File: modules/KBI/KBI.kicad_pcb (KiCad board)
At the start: 2 copper layers, 100 x 130 mm, 45 parts, among them IC3 µA741C, IC4 µA741C, J1 +15V, J2 -15V, J3 GND, J4 KOV, J5 GATE, J6 FM, P1 1M, P2 100k, P3 100k, P4 100k, P5 100k, T1 N-FET, T2 N-FET, T3 N-FET, T4 N-FET

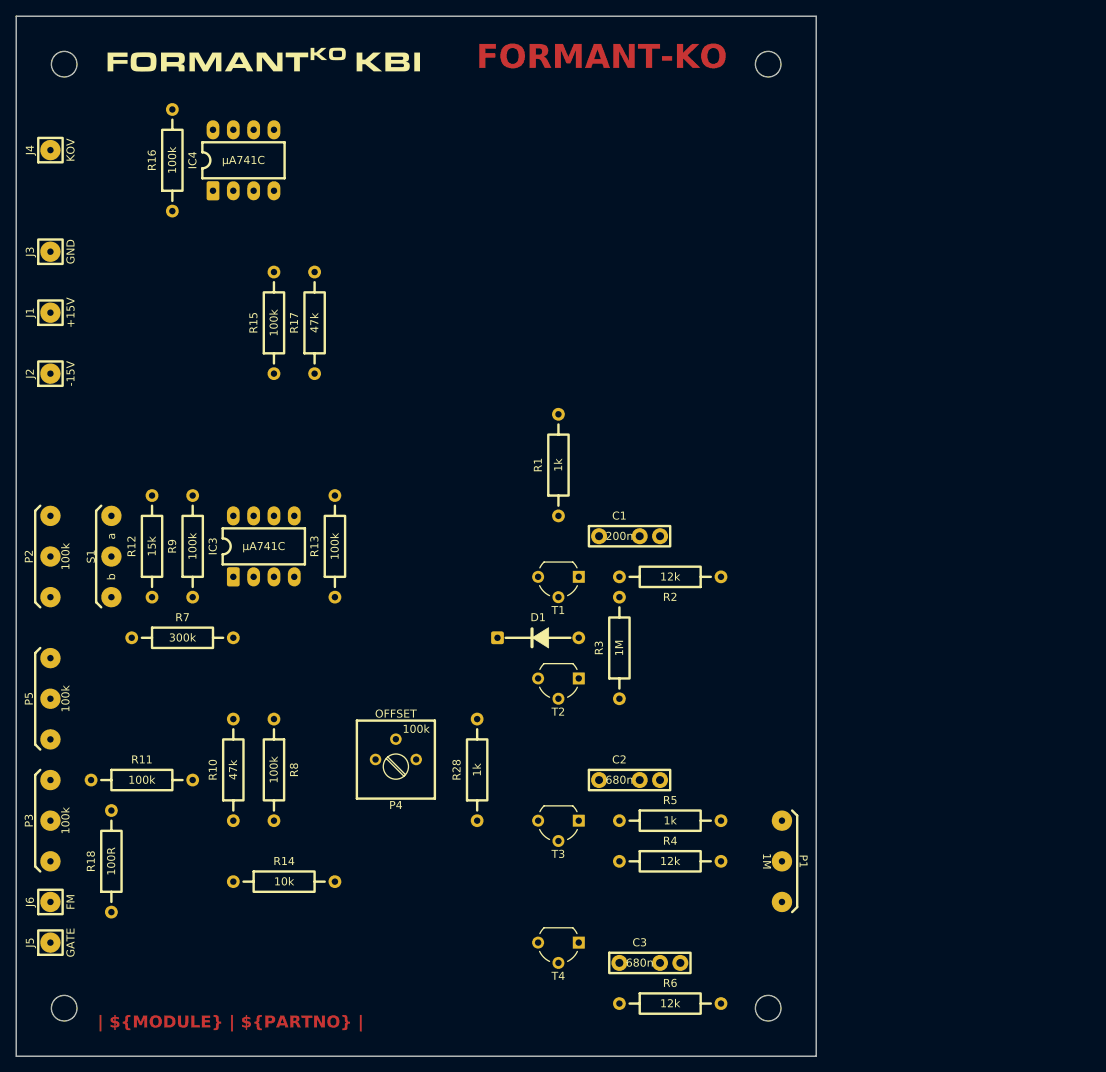
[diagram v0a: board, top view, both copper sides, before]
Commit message: initialized 6U modules
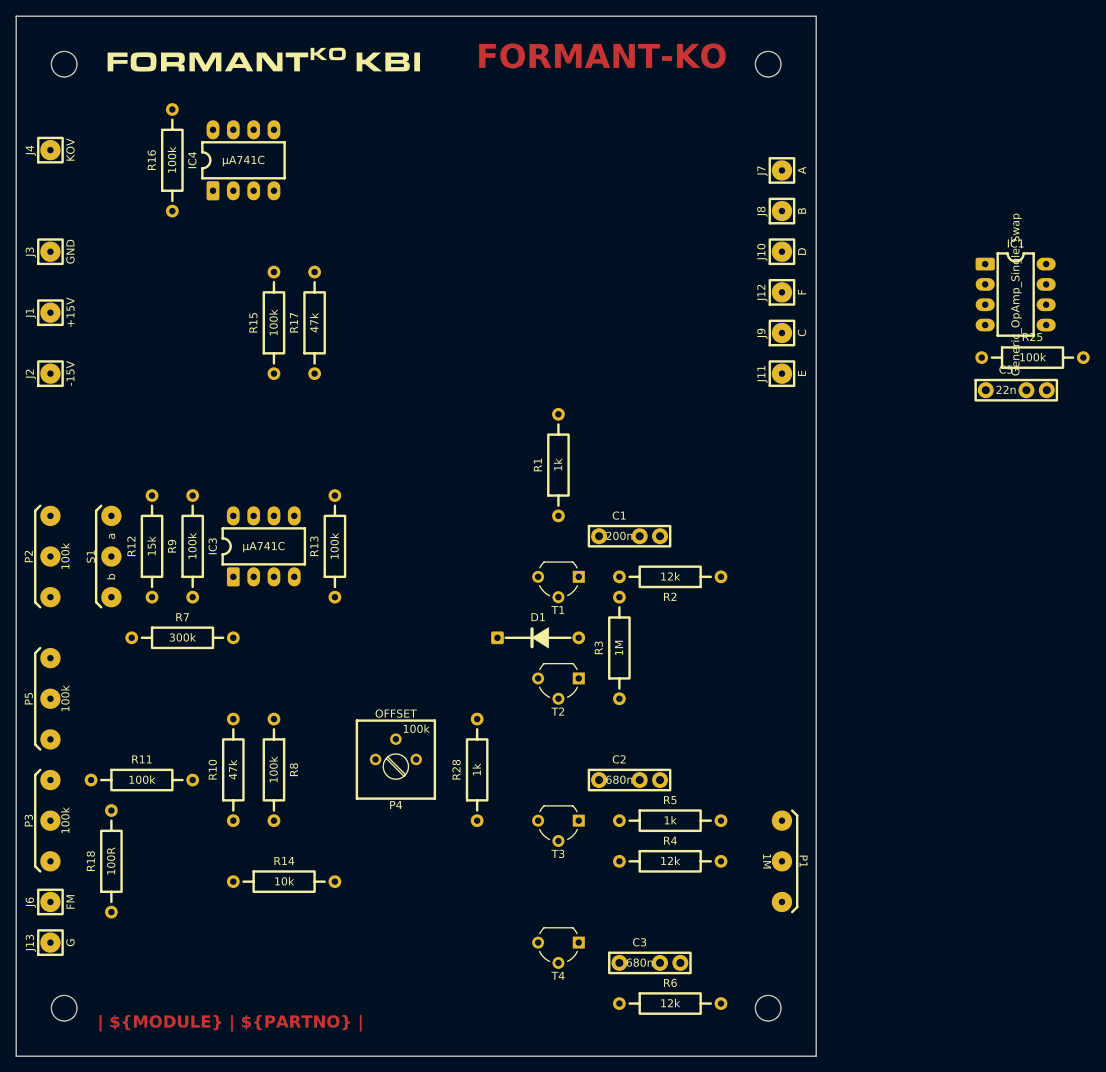
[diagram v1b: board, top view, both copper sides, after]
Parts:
- removed J5: GATE, FormantKO:Wire_1x01_General
- added C5: 22n, FormantKO:C_Disc, F.Cu at (215.3, 79.5)
- added IC1: Generic_OpAmp_Single_Swap, FormantKO:DIP-8, F.Cu at (216.5, 67.5)
- added J10: D, FormantKO:Wire_1x01_General, F.Cu at (187.3, 62.2)
- added J11: E, FormantKO:Wire_1x01_General, F.Cu at (187.3, 77.4)
- added J12: F, FormantKO:Wire_1x01_General, F.Cu at (187.3, 67.2)
- added J13: G, FormantKO:Wire_1x01_General, F.Cu at (95.9, 148.5)
- added J7: A, FormantKO:Wire_1x01_General, F.Cu at (187.3, 52.0)
- added J8: B, FormantKO:Wire_1x01_General, F.Cu at (187.3, 57.1)
- added J9: C, FormantKO:Wire_1x01_General, F.Cu at (187.3, 72.3)
- added R25: 100k, FormantKO:R_Axial_Horizontal, F.Cu at (218.6, 75.4)
